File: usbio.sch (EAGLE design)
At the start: 19 parts, among them U1 ATMEGA328P-MU-QFN32

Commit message: Comartiment schematic
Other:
- note added: "LEDs"
- note added: "Other Periphery"
- note removed: "Please notice 3v3 is connected to 5v."
- moved on the sheet: C1, C9, D1, D2, IC2, JP1, LED1, LED5, LED6, R1A, R1B, R1C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

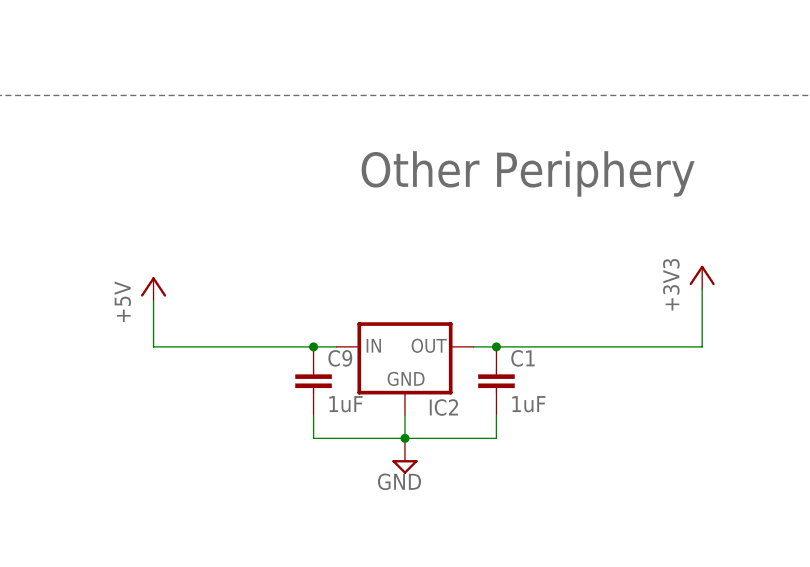
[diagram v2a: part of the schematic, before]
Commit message: Add LDO bypass jumper
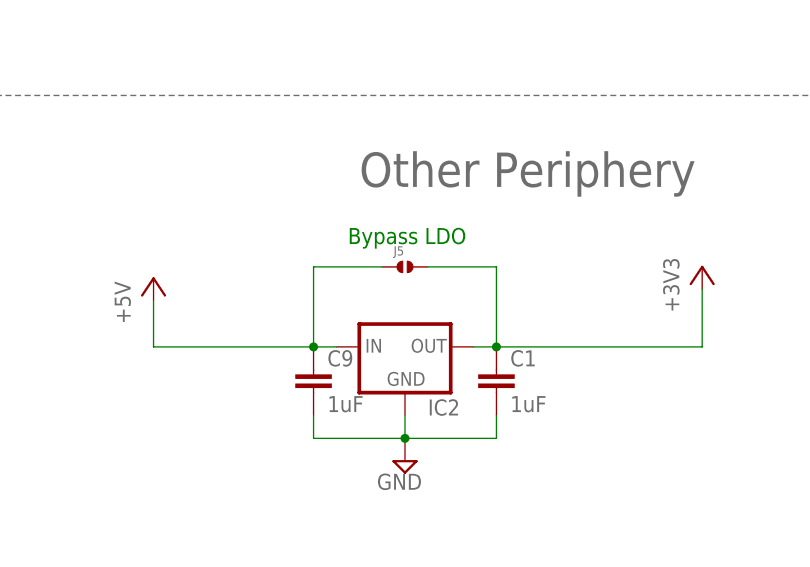
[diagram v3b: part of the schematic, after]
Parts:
- added J5: (no value), solderjumper:SOLDERJUMPER.2.MED
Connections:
- net +3V3: now also J5.2
- net +5V: now also J5.1
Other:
- note added: "Bypass LDO"
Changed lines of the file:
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@@
 <setting verticaltext="up"/>
 </settings>
-<grid distance="0.1" unitdist="inch" unit="inch" style="lines" multiple="1" display="no" altdistance="0.01" altunitdist="inch" altunit="inch"/>
+<grid distance="0.05" unitdist="inch" unit="inch" style="lines" multiple="1" display="no" altdistance="0.01" altunitdist="inch" altunit="inch"/>
 <layers>
 <layer number="1" name="Top" color="4" fill="1" visible="no" active="no"/>
@@
 <part name="C9" library="rcl" deviceset="C-EU" device="C0603" value="1uF"/>
 <part name="P+1" library="supply1" deviceset="+5V" device=""/>
+<part name="J5" library="solderjumper" deviceset="SOLDERJUMPER.2" device=".MED"/>
 </parts>
 <sheets>
@@
 <text x="251.46" y="114.3" size="3.81" layer="95">Other Periphery</text>
 <text x="134.62" y="116.84" size="3.81" layer="95">LEDs</text>
+<text x="250.19" y="107.95" size="1.778" layer="91">Bypass LDO</text>
 </plain>
 <instances>
@@
 <instance part="P+1" gate="1" x="243.84" y="193.04" smashed="yes" rot="R270">
 <attribute name="VALUE" x="238.76" y="195.58" size="1.778" layer="96"/>
+</instance>
+<instance part="J5" gate="G$1" x="256.54" y="105.41" smashed="yes">
+<attribute name="NAME" x="255.27" y="106.68" size="1.016" layer="95"/>
+<attribute name="VALUE" x="255.27" y="102.87" size="1.016" layer="96"/>
 </instance>
 </instances>
@@
 <wire x1="289.56" y1="96.52" x2="266.7" y2="96.52" width="0.1524" layer="91"/>
 <junction x="266.7" y="96.52"/>
+<pinref part="J5" gate="G$1" pin="2"/>
+<wire x1="259.08" y1="105.41" x2="266.7" y2="105.41" width="0.1524" layer="91"/>
+<wire x1="266.7" y1="105.41" x2="266.7" y2="96.52" width="0.1524" layer="91"/>
 </segment>
 </net>
@@
 <pinref part="C9" gate="G$1" pin="1"/>
 <junction x="246.38" y="96.52"/>
-</segment>
-<segment>
+<pinref part="J5" gate="G$1" pin="1"/>
+<wire x1="254" y1="105.41" x2="246.38" y2="105.41" width="0.1524" layer="91"/>
+<wire x1="246.38" y1="105.41" x2="246.38" y2="96.52" width="0.1524" layer="91"/>
+</segment>
+<segment>

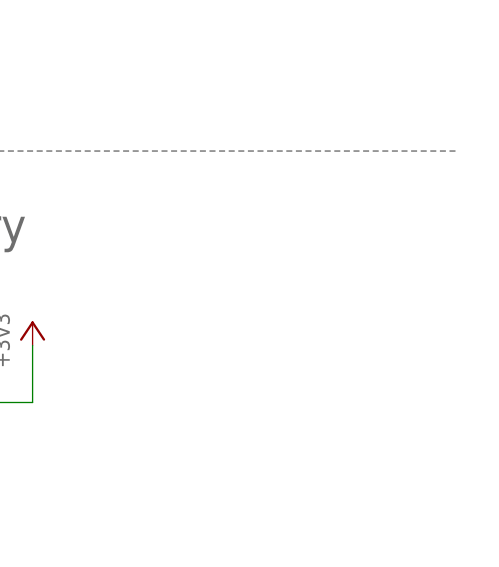
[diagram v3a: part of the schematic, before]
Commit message: Add pullup on RST
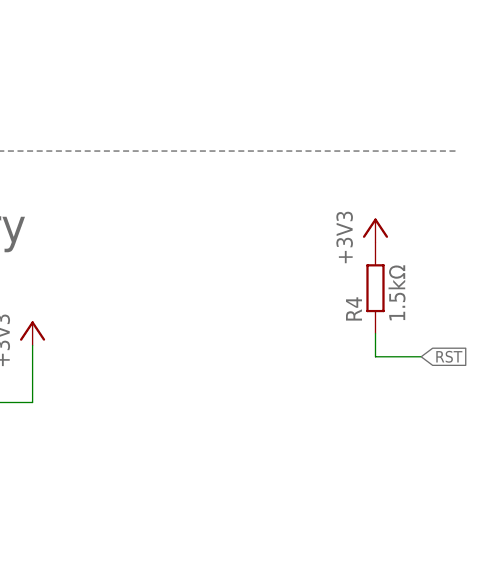
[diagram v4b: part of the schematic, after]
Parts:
- added R4: 1.5kΩ, rcl:R-EU_R0603
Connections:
- net +3V3: now also R4.2
- net RST: now also R4.1
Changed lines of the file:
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@@
 <setting verticaltext="up"/>
 </settings>
-<grid distance="0.05" unitdist="inch" unit="inch" style="lines" multiple="1" display="no" altdistance="0.01" altunitdist="inch" altunit="inch"/>
+<grid distance="0.1" unitdist="inch" unit="inch" style="lines" multiple="1" display="no" altdistance="0.01" altunitdist="inch" altunit="inch"/>
 <layers>
 <layer number="1" name="Top" color="4" fill="1" visible="no" active="no"/>
@@
 <part name="P+1" library="supply1" deviceset="+5V" device=""/>
 <part name="J5" library="solderjumper" deviceset="SOLDERJUMPER.2" device=".MED"/>
+<part name="R4" library="rcl" deviceset="R-EU_" device="R0603" value="1.5kΩ"/>
+<part name="+3V1" library="supply1" deviceset="+3V3" device=""/>
 </parts>
 <sheets>
@@
 <attribute name="VALUE" x="255.27" y="102.87" size="1.016" layer="96"/>
 </instance>
+<instance part="R4" gate="G$1" x="327.66" y="109.22" smashed="yes" rot="R90">
+<attribute name="NAME" x="326.1614" y="105.41" size="1.778" layer="95" rot="R90"/>
+<attribute name="VALUE" x="330.962" y="105.41" size="1.778" layer="96" rot="R90"/>
+</instance>
+<instance part="+3V1" gate="G$1" x="327.66" y="116.84" smashed="yes">
+<attribute name="VALUE" x="325.12" y="111.76" size="1.778" layer="96" rot="R90"/>
+</instance>
 </instances>
 <busses>
@@
 <wire x1="266.7" y1="105.41" x2="266.7" y2="96.52" width="0.1524" layer="91"/>
 </segment>
+<segment>
+<pinref part="R4" gate="G$1" pin="2"/>
+<pinref part="+3V1" gate="G$1" pin="+3V3"/>
+</segment>
 </net>
 <net name="ADCENA" class="0">
@@
 <label x="241.3" y="58.42" size="1.27" layer="95" rot="R180" xref="yes"/>
 </segment>
-</net>
+<segment>
+<pinref part="R4" gate="G$1" pin="1"/>
+<wire x1="327.66" y1="104.14" x2="327.66" y2="101.6" width="0.1524" layer="91"/>
+<wire x1="327.66" y1="101.6" x2="332.74" y2="101.6" width="0.1524" layer="91"/>
+<label x="332.74" y="101.6" size="1.27" layer="95" xref="yes"/>
+</segment>
+</net>
